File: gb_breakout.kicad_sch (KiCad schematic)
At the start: 13 parts

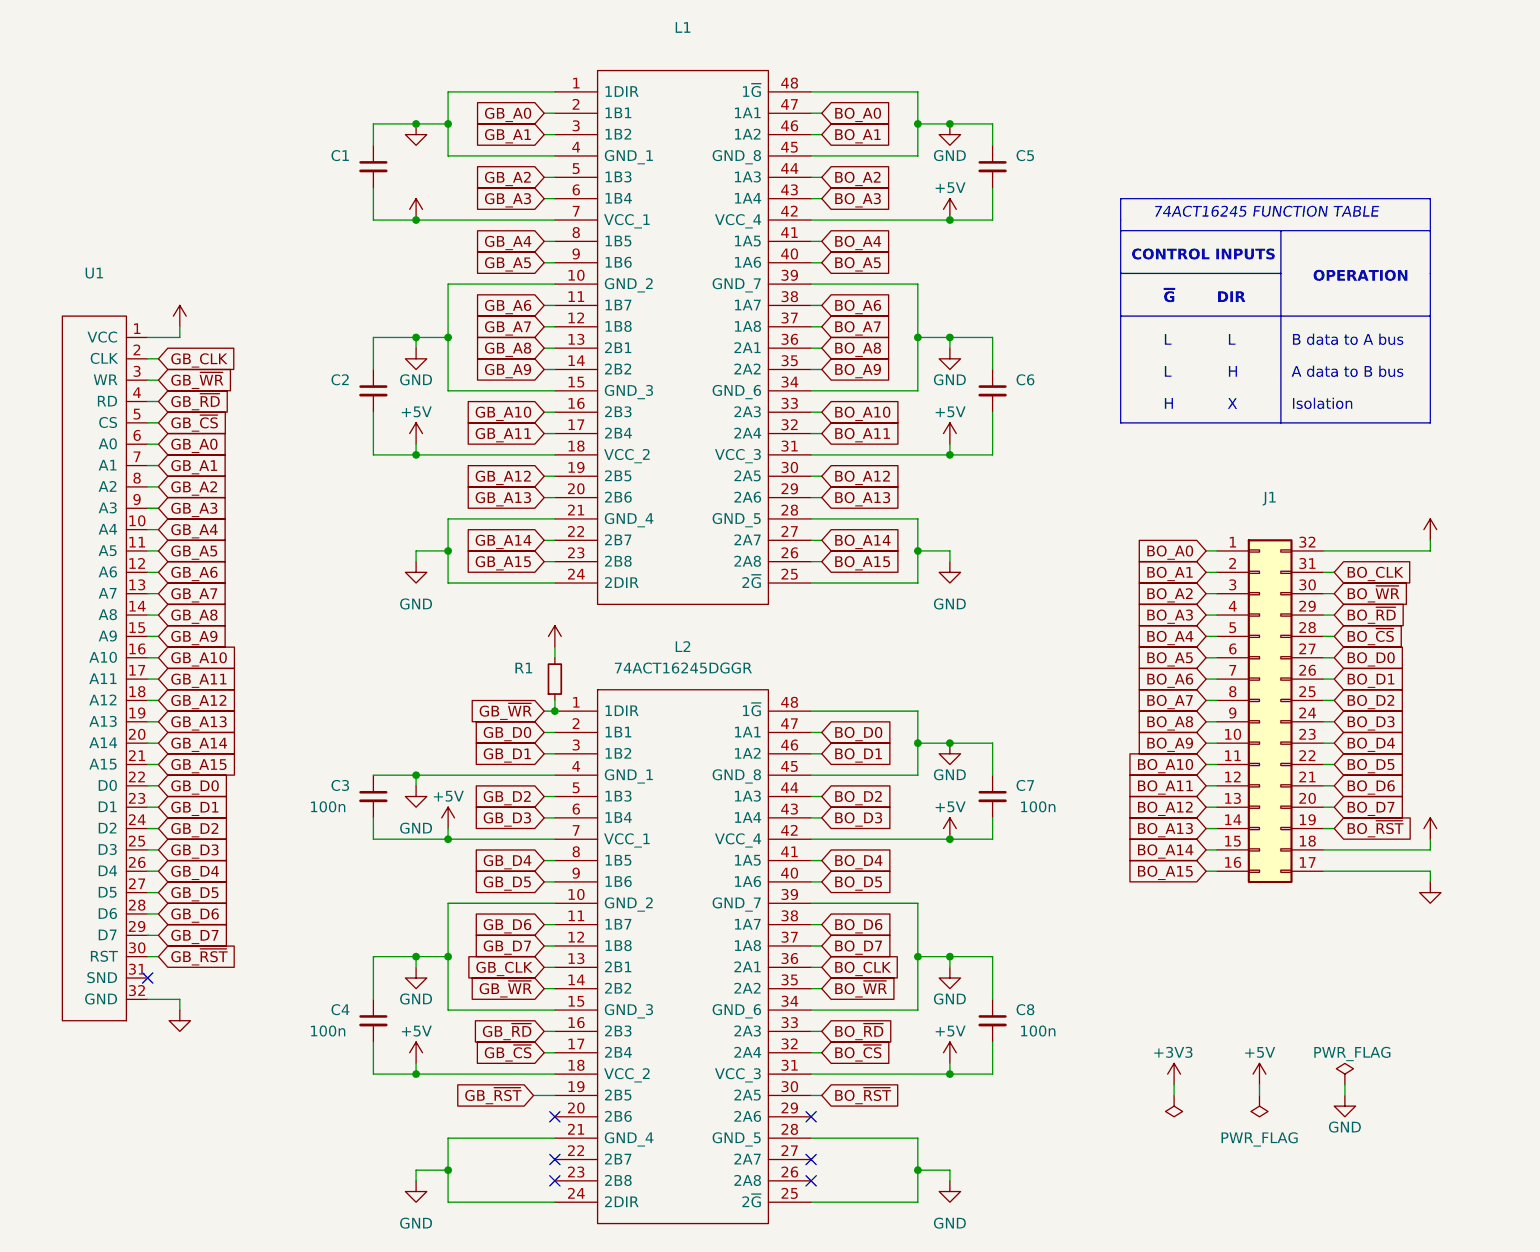
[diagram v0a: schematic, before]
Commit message: add libs + fix associations
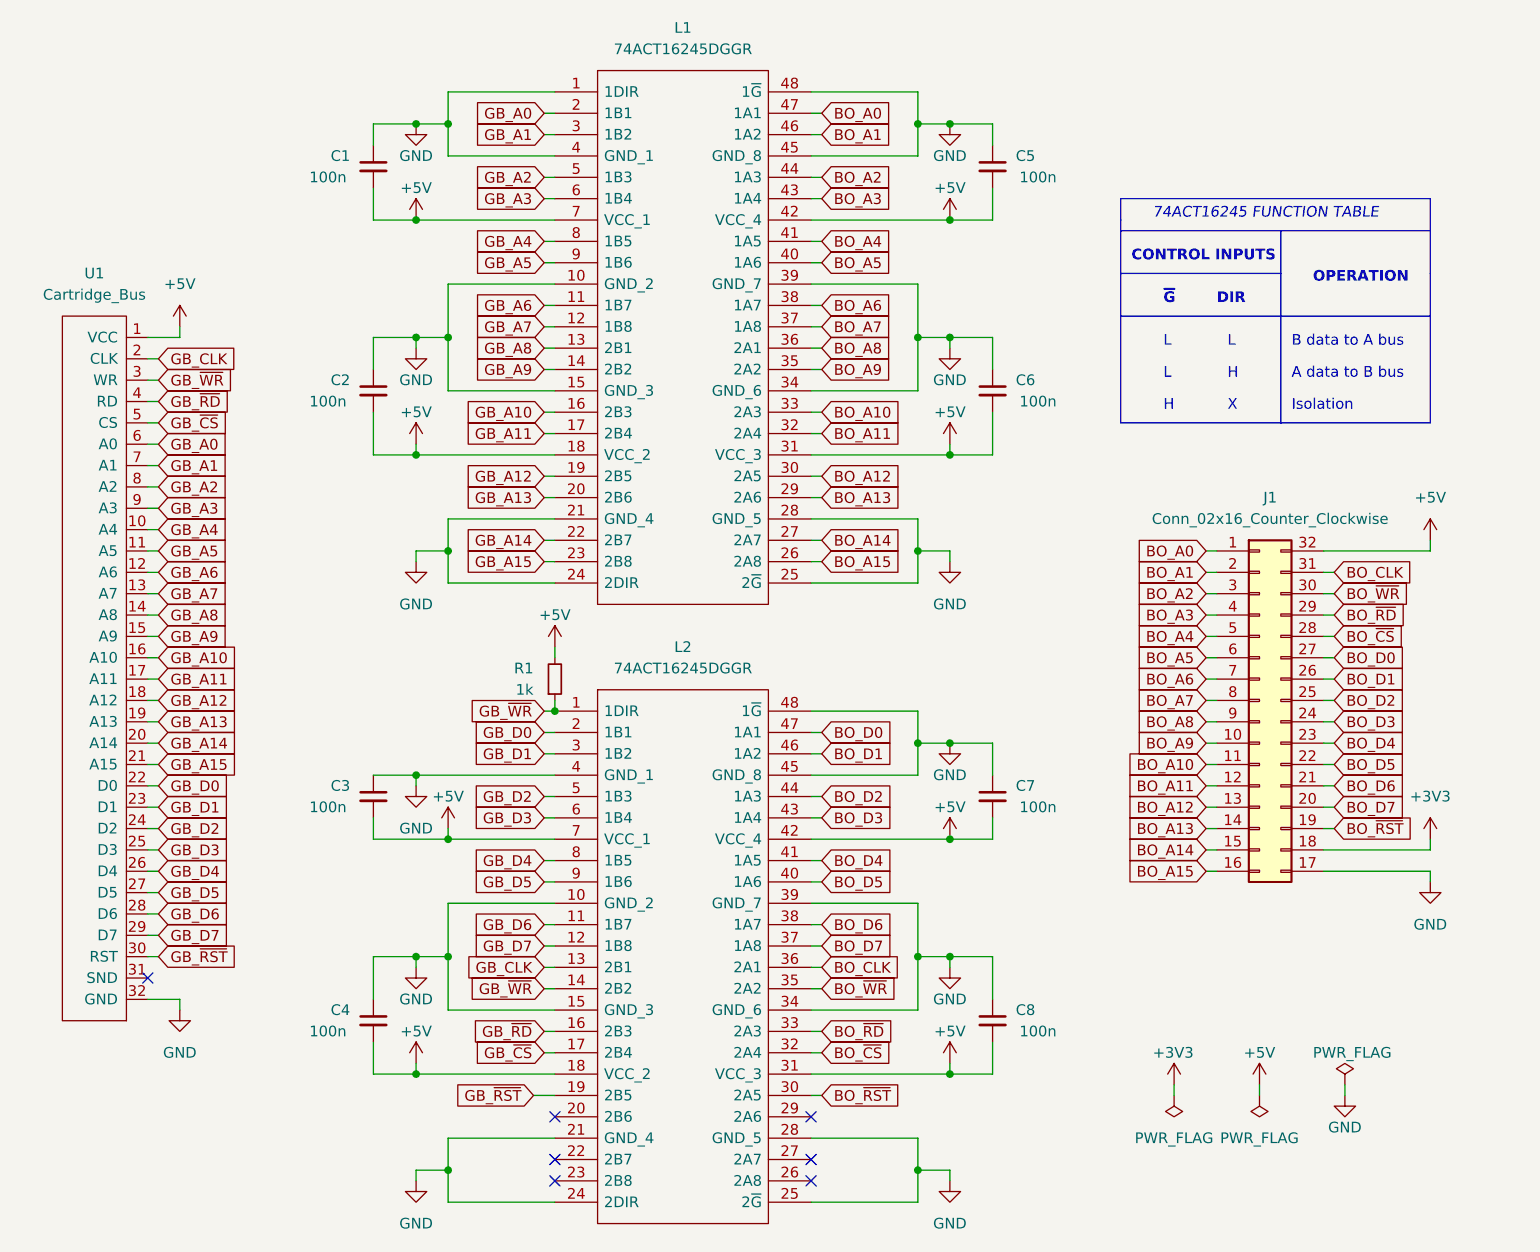
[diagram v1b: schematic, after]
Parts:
- removed L1: (no value), symbol SamacSys_Parts:74ACT16245DGGR
- removed L2: 74ACT16245DGGR, symbol SamacSys_Parts:74ACT16245DGGR
- added L1, L2: 74ACT16245DGGR, 74ACT16245DGGR:SOP50P810X120-48N, symbol 74ACT16245DGGR:74ACT16245DGGR
- C1, C2, C5, C6: value (none) -> 100n; footprint (none) -> Capacitor_SMD:C_0201_0603Metric
- C3, C4, C7, C8: footprint (none) -> Capacitor_SMD:C_0201_0603Metric
- J1: value (none) -> Conn_02x16_Counter_Clockwise; footprint (none) -> Connector_PinHeader_2.54mm:PinHeader_2x16_P2.54mm_Vertical_SMD
- R1: value (none) -> 1k; footprint (none) -> Resistor_SMD:R_0201_0603Metric
- U1: value (none) -> Cartridge_Bus; footprint (none) -> HDR_Gameboy_Cartridges:GB_Cartridge
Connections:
- net +5V: now also L1.18 (VCC_2), L1.31 (VCC_3), L1.42 (VCC_4), L1.7 (VCC_1), L2.18 (VCC_2), L2.31 (VCC_3), L2.42 (VCC_4), L2.7 (VCC_1)
- net BO_A0: now also L1.47 (1A1)
- net BO_A1: now also L1.46 (1A2)
- net BO_A10: now also L1.33 (2A3)
- net BO_A11: now also L1.32 (2A4)
- net BO_A12: now also L1.30 (2A5)
- net BO_A13: now also L1.29 (2A6)
- net BO_A14: now also L1.27 (2A7)
- net BO_A15: now also L1.26 (2A8)
- net BO_A2: now also L1.44 (1A3)
- net BO_A3: now also L1.43 (1A4)
- net BO_A4: now also L1.41 (1A5)
- net BO_A5: now also L1.40 (1A6)
- net BO_A6: now also L1.38 (1A7)
- net BO_A7: now also L1.37 (1A8)
- net BO_A8: now also L1.36 (2A1)
- net BO_A9: now also L1.35 (2A2)
- net BO_CLK: now also L2.36 (2A1)
- net BO_D0: now also L2.47 (1A1)
- net BO_D1: now also L2.46 (1A2)
- net BO_D2: now also L2.44 (1A3)
- net BO_D3: now also L2.43 (1A4)
- net BO_D4: now also L2.41 (1A5)
- net BO_D5: now also L2.40 (1A6)
- net BO_D6: now also L2.38 (1A7)
- net BO_D7: now also L2.37 (1A8)
- net BO_~{CS}: now also L2.32 (2A4)
- net BO_~{RD}: now also L2.33 (2A3)
- net BO_~{RST}: now also L2.30 (2A5)
- net BO_~{WR}: now also L2.35 (2A2)
- net GB_A0: now also L1.2 (1B1)
- net GB_A1: now also L1.3 (1B2)
- net GB_A10: now also L1.16 (2B3)
- net GB_A11: now also L1.17 (2B4)
- net GB_A12: now also L1.19 (2B5)
- net GB_A13: now also L1.20 (2B6)
- net GB_A14: now also L1.22 (2B7)
- net GB_A15: now also L1.23 (2B8)
- net GB_A2: now also L1.5 (1B3)
- net GB_A3: now also L1.6 (1B4)
- net GB_A4: now also L1.8 (1B5)
- net GB_A5: now also L1.9 (1B6)
- net GB_A6: now also L1.11 (1B7)
- net GB_A7: now also L1.12 (1B8)
- net GB_A8: now also L1.13 (2B1)
- net GB_A9: now also L1.14 (2B2)
- net GB_CLK: now also L2.13 (2B1)
- net GB_D0: now also L2.2 (1B1)
- net GB_D1: now also L2.3 (1B2)
- net GB_D2: now also L2.5 (1B3)
- net GB_D3: now also L2.6 (1B4)
- net GB_D4: now also L2.8 (1B5)
- net GB_D5: now also L2.9 (1B6)
- net GB_D6: now also L2.11 (1B7)
- net GB_D7: now also L2.12 (1B8)
- net GB_~{CS}: now also L2.17 (2B4)
- net GB_~{RD}: now also L2.16 (2B3)
- net GB_~{RST}: now also L2.19 (2B5)
- net GB_~{WR}: now also L2.1 (1DIR), L2.14 (2B2)
- net GND: now also L1.1 (1DIR), L1.10 (GND_2), L1.15 (GND_3), L1.21 (GND_4), L1.24 (2DIR), L1.25 (2~{G}), L1.28 (GND_5), L1.34 (GND_6), L1.39 (GND_7), L1.4 (GND_1), L1.45 (GND_8), L1.48 (1~{G}), L2.10 (GND_2), L2.15 (GND_3), L2.21 (GND_4), L2.24 (2DIR), L2.25 (2~{G}), L2.28 (GND_5), L2.34 (GND_6), L2.39 (GND_7), L2.4 (GND_1), L2.45 (GND_8), L2.48 (1~{G})

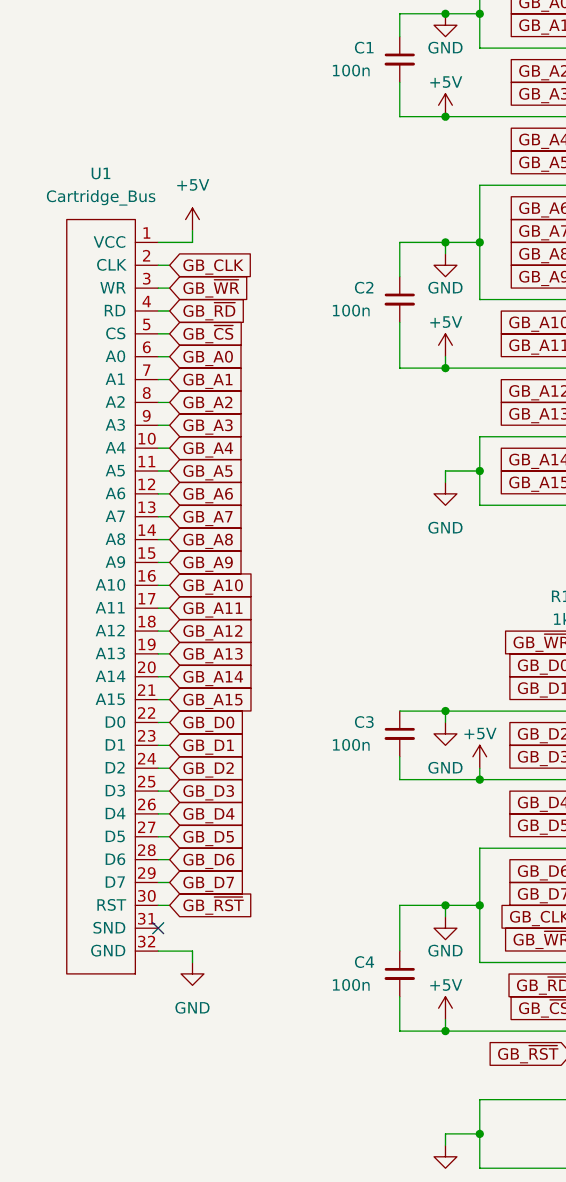
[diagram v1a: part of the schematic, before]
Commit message: finished power+gnd routing
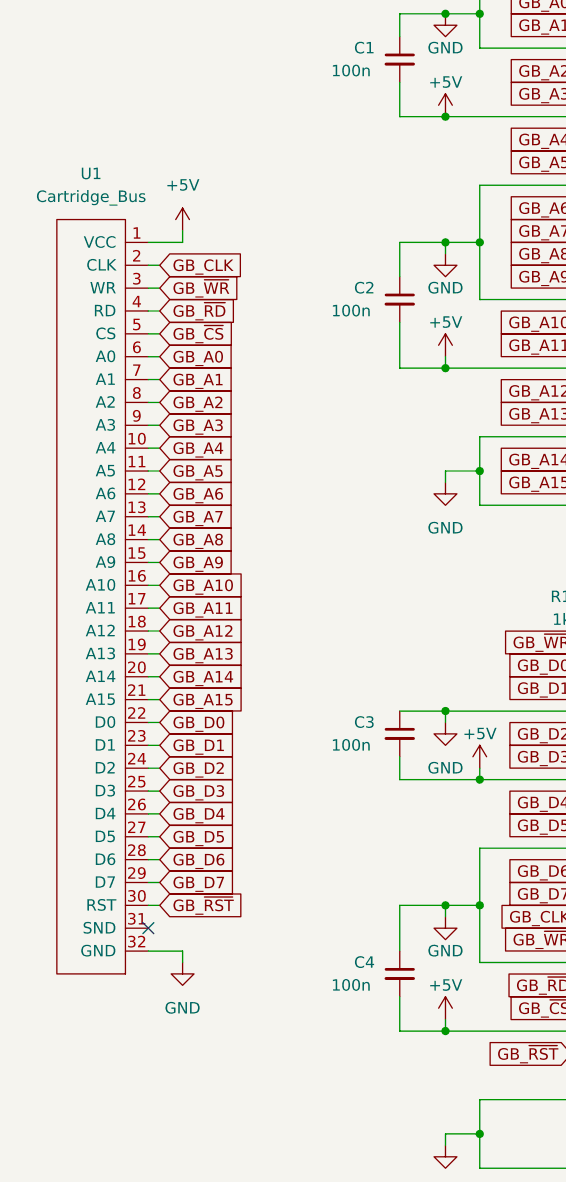
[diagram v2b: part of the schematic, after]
